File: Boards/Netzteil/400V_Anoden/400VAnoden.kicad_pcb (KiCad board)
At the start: 2 copper layers, 160 x 100 mm, 51 parts, among them P1 Drossel, P2 320V_AC, P3 Stabi, P4 133V_AC, P5 Stabi, P6 Trafo, P7 Trafo, P8 Relay, Q1 2SC2979

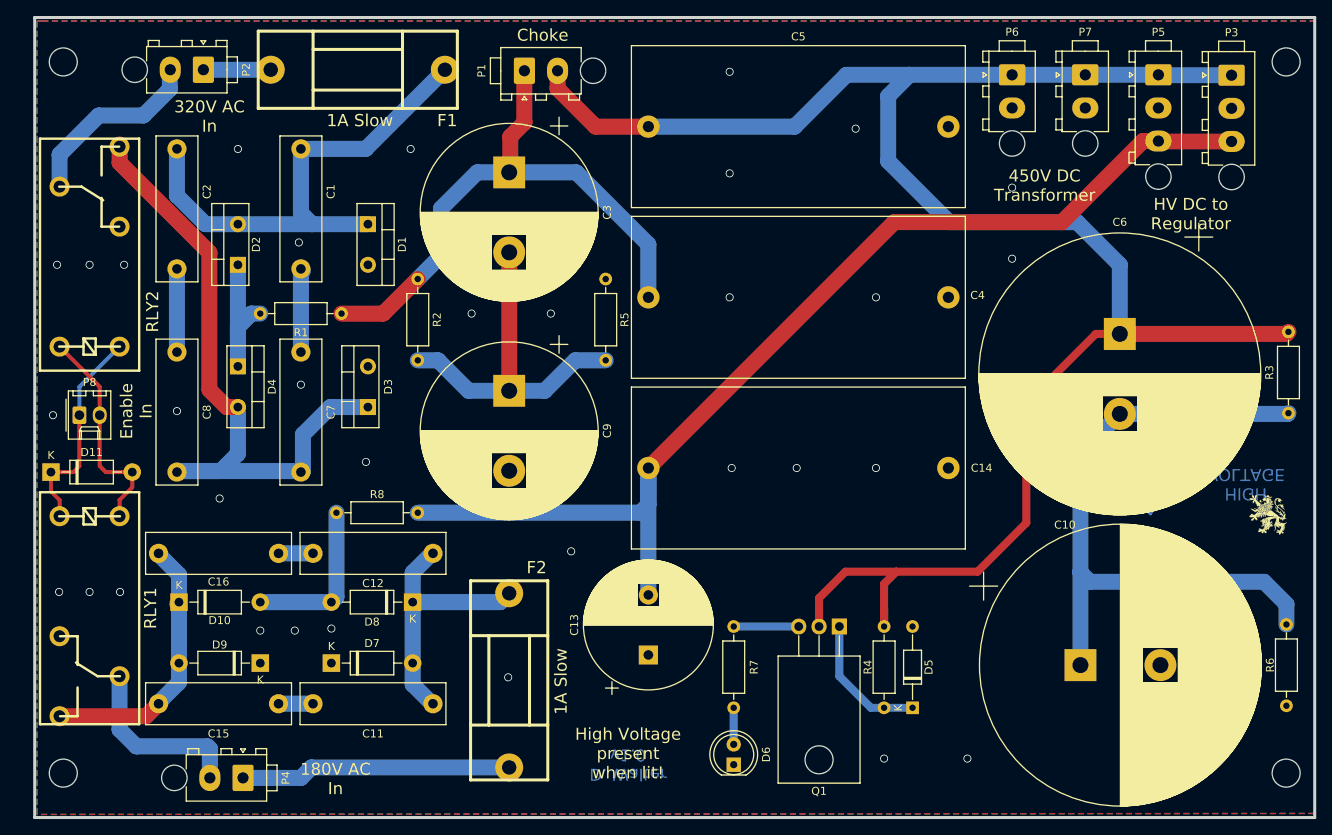
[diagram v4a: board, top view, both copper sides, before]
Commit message: Adjusted Silkscreen
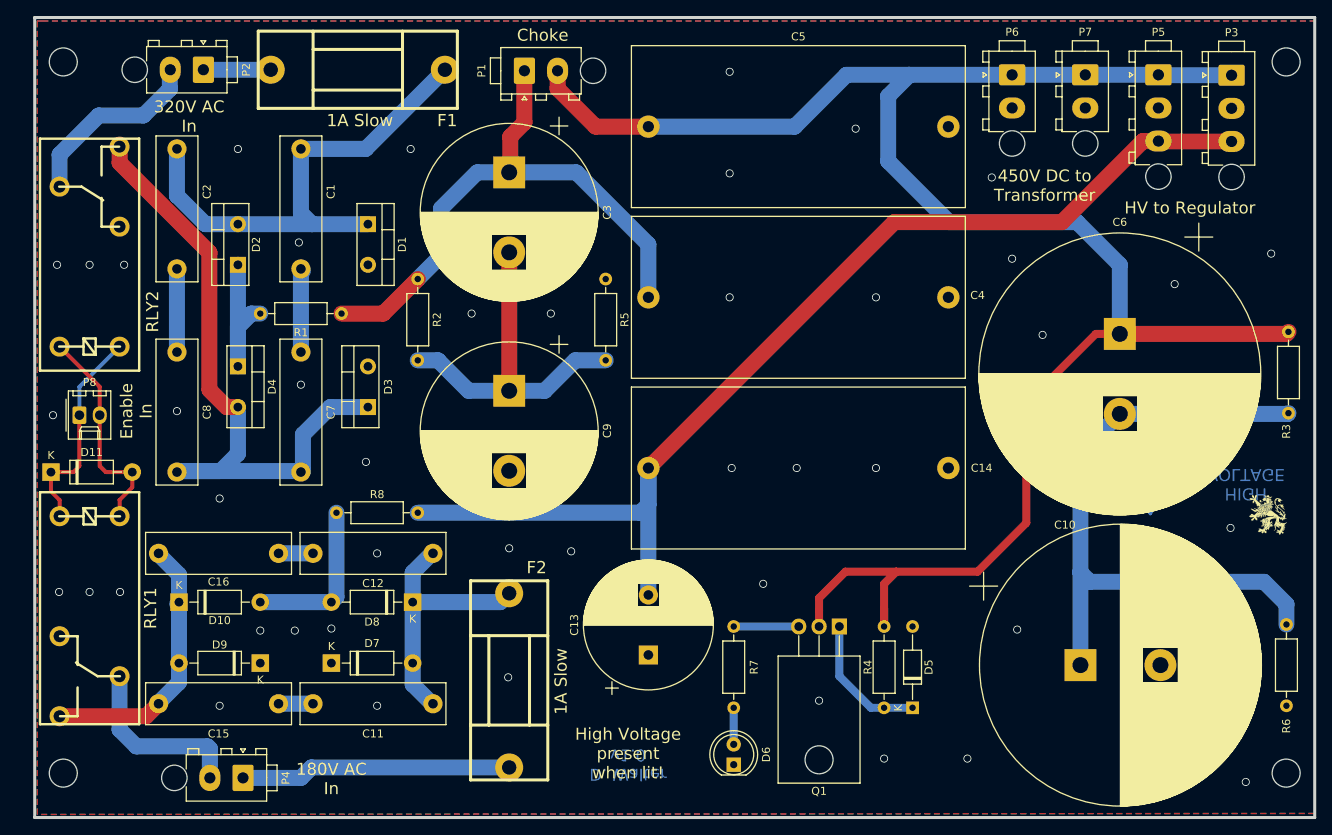
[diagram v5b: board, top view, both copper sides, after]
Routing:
- net GND: vias 33 -> 45
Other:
- board text added: "450V DC to Transformer"
- board text added: "HV to Regulator"
- board text removed: "450V DC Transformer"
- board text removed: "HV DC to Regulator"
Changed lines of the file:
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@@
     (thickness 1.6)
     (drawings 9)
-    (tracks 192)
+    (tracks 204)
     (zones 0)
     (modules 51)
@@
   (page A4)
   (layers
-    (0 F.Cu signal)
-    (31 B.Cu signal)
+    (0 F.Cu signal hide)
+    (31 B.Cu signal hide)
     (32 B.Adhes user)
     (33 F.Adhes user)
@@
     (descr "Resistor, Axial_DIN0207 series, Axial, Horizontal, pin pitch=10.16mm, 0.25W = 1/4W, length*diameter=6.3*2.5mm^2, http://cdn-reichelt.de/documents/datenblatt/B400/1_4W%23YAG.pdf")
     (tags "Resistor Axial_DIN0207 series Axial Horizontal pin pitch 10.16mm 0.25W = 1/4W length 6.3mm diameter 2.5mm")
-    (fp_text reference R6 (at 5.08 -2.032 90) (layer F.SilkS)
+    (fp_text reference R6 (at -2.54 0 90) (layer F.SilkS)
       (effects (font (size 1 1) (thickness 0.15)))
     )
@@
     (descr "Resistor, Axial_DIN0207 series, Axial, Horizontal, pin pitch=10.16mm, 0.25W = 1/4W, length*diameter=6.3*2.5mm^2, http://cdn-reichelt.de/documents/datenblatt/B400/1_4W%23YAG.pdf")
     (tags "Resistor Axial_DIN0207 series Axial Horizontal pin pitch 10.16mm 0.25W = 1/4W length 6.3mm diameter 2.5mm")
-    (fp_text reference R3 (at 5.08 -2.37 90) (layer F.SilkS)
+    (fp_text reference R3 (at -2.286 -0.254 90) (layer F.SilkS)
       (effects (font (size 1 1) (thickness 0.15)))
     )
@@
     )
   )
-  (gr_text "320V AC\nIn" (at 58.42 39.37) (layer F.SilkS)
+  (gr_text "320V AC\nIn" (at 55.88 39.37) (layer F.SilkS)
     (effects (font (size 1.5 1.5) (thickness 0.3)))
   )
-  (gr_text "180V AC\nIn" (at 74.168 122.174) (layer F.SilkS)
+  (gr_text "180V AC\nIn" (at 73.66 122.174) (layer F.SilkS)
     (effects (font (size 1.5 1.5) (thickness 0.3)))
   )
@@
     (effects (font (size 1.5 1.5) (thickness 0.3)))
   )
-  (gr_text "HV DC to\nRegulator" (at 181.102 51.562) (layer F.SilkS)
+  (gr_text "HV to Regulator" (at 180.975 50.8) (layer F.SilkS)
     (effects (font (size 1.5 1.5) (thickness 0.3)))
   )
-  (gr_text "450V DC\nTransformer" (at 162.814 48.006) (layer F.SilkS)
+  (gr_text "450V DC to\nTransformer" (at 162.814 48.006) (layer F.SilkS)
     (effects (font (size 1.5 1.5) (thickness 0.3)))
   )
@@
   (via (at 123.444 46.482) (size 1) (drill 0.8) (layers F.Cu B.Cu) (net 6))
   (via (at 123.444 33.782) (size 1) (drill 0.8) (layers F.Cu B.Cu) (net 6))
-  (via (at 158.75 48.26) (size 1) (drill 0.8) (layers F.Cu B.Cu) (net 6))
+  (via (at 156.21 46.99) (size 1) (drill 0.8) (layers F.Cu B.Cu) (net 6))
   (via (at 158.75 57.15) (size 1) (drill 0.8) (layers F.Cu B.Cu) (net 6))
   (via (at 64.77 103.632) (size 1) (drill 0.8) (layers F.Cu B.Cu) (net 6))
@@
   (via (at 153.162 119.634) (size 1) (drill 0.8) (layers F.Cu B.Cu) (net 6))
   (via (at 38.862 76.708) (size 1) (drill 0.8) (layers F.Cu B.Cu) (net 6))
+  (via (at 191.135 56.515) (size 1) (drill 0.8) (layers F.Cu B.Cu) (net 6))
+  (via (at 186.055 90.805) (size 1) (drill 0.8) (layers F.Cu B.Cu) (net 6))
+  (via (at 187.96 122.555) (size 1) (drill 0.8) (layers F.Cu B.Cu) (net 6))
+  (via (at 127.635 97.79) (size 1) (drill 0.8) (layers F.Cu B.Cu) (net 6))
+  (via (at 95.885 93.345) (size 1) (drill 0.8) (layers F.Cu B.Cu) (net 6))
+  (via (at 79.375 93.98) (size 1) (drill 0.8) (layers F.Cu B.Cu) (net 6))
+  (via (at 79.375 113.03) (size 1) (drill 0.8) (layers F.Cu B.Cu) (net 6))
+  (via (at 59.69 113.03) (size 1) (drill 0.8) (layers F.Cu B.Cu) (net 6))
+  (via (at 134.62 112.395) (size 1) (drill 0.8) (layers F.Cu B.Cu) (net 6))
+  (via (at 159.385 103.505) (size 1) (drill 0.8) (layers F.Cu B.Cu) (net 6))
+  (via (at 162.56 66.675) (size 1) (drill 0.8) (layers F.Cu B.Cu) (net 6))
+  (via (at 179.07 60.325) (size 1) (drill 0.8) (layers F.Cu B.Cu) (net 6))
   (segment (start 172.212 76.548) (end 167.292 81.468) (width 2) (layer B.Cu) (net 7) (status 10))
   (segment (start 193.2 76.548) (end 193.294 76.454) (width 2) (layer B.Cu) (net 7) (status 30))

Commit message: Added Mounting holes, Moved -60V Divider to HV Board, eliminated +450V Connector and Feedback Connector on Amp Board
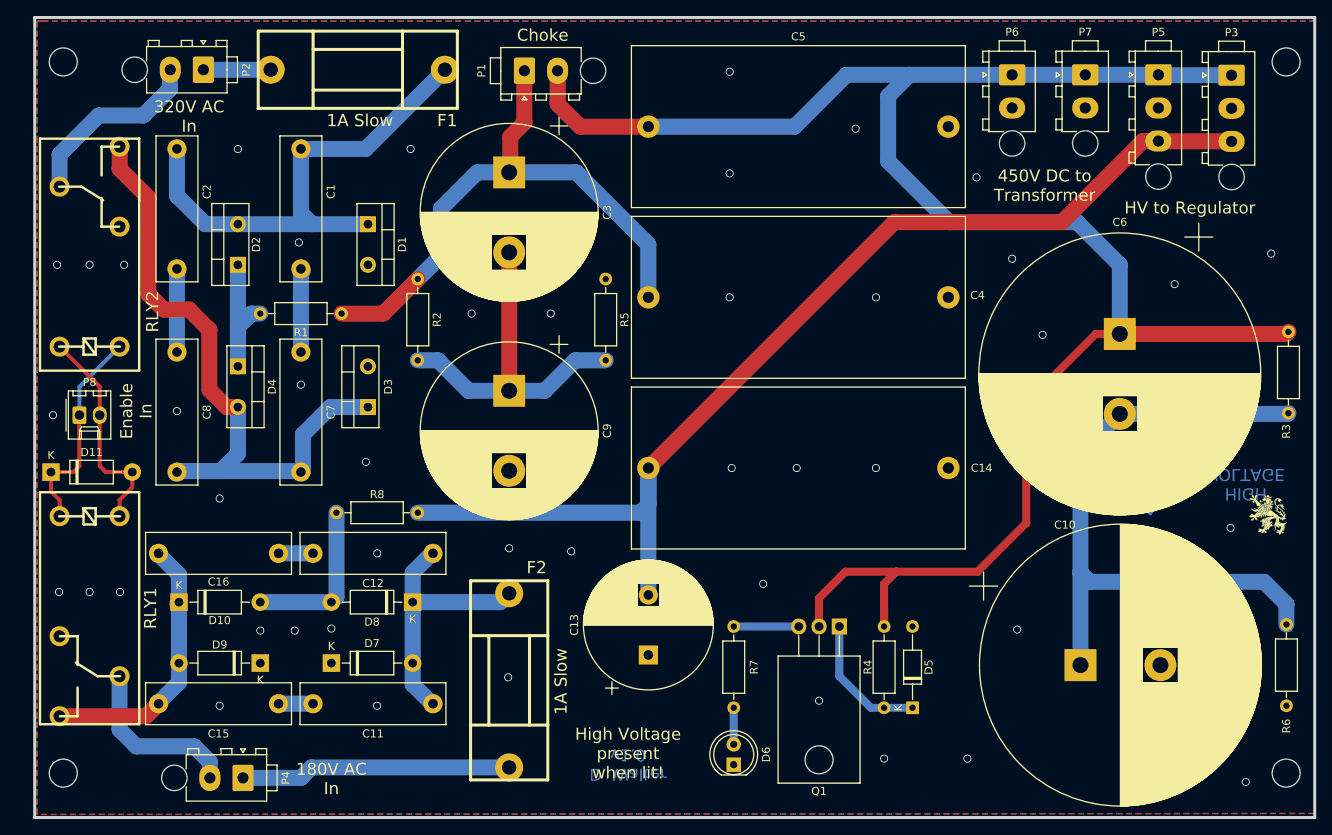
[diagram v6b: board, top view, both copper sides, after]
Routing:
- net Net-(C7-Pad2): track 83.7 -> 85.6 mm
- net /+450V_DC: track 240.0 -> 241.1 mm
- net Net-(P4-Pad2): track 22.6 -> 21.6 mm

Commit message: 6,3V und 12V auf einer Platine zusammengefasst
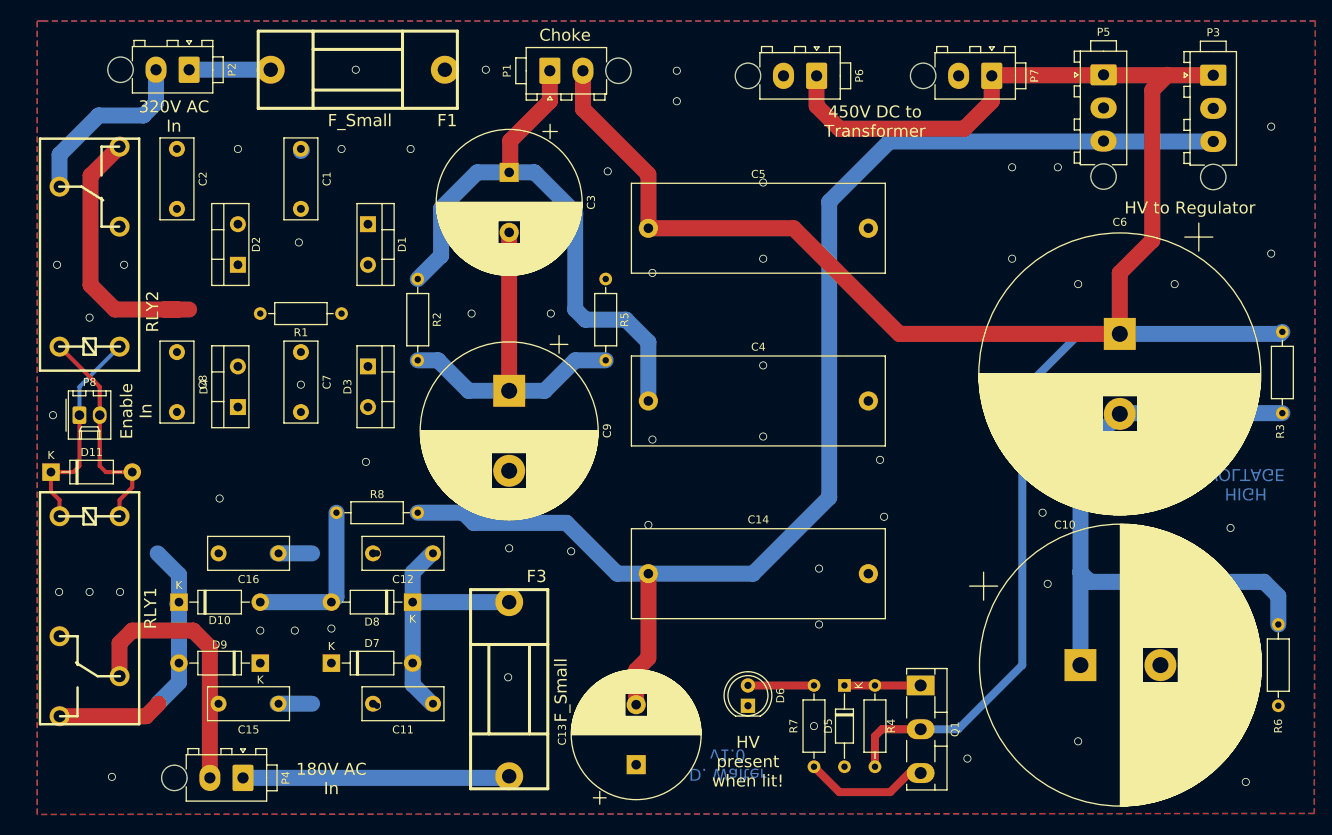
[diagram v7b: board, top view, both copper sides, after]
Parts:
- removed F2: 1A Slow, w_misc_comp:fuse_holder_CQ-2
- removed G***: LOGO, Loewe:Loewe_Klein
- removed REF**: Symbol_HighVoltage_Type2_CopperTop_VerySmall, Symbol:Symbol_HighVoltage_Type2_CopperTop_VerySmall
- removed REF**: EuroBoard160mmX100mm_holes, EuroBoard_Outline:EuroBoard160mmX100mm_holes
- added F3: F_Small, w_misc_comp:fuse_holder_CQ-2, F.Cu at (95.9, 111.0)
- C1, C11, C12, C15, C16, C2, C7, C8: value 1nF -> 1nF/450V; footprint Capacitor_THT:C_Rect_L18.0mm_W5.0mm_P15.00mm_FKS3_FKP3 -> Capacitor_THT:C_Rect_L10.0mm_W4.0mm_P7.50mm_FKS3_FKP3
- C14: value 1µF/600V -> 1µF/630V; footprint Capacitor_THT:C_Rect_L41.5mm_W20.0mm_P37.50mm_MKS4 -> Capacitor_THT:C_Rect_L31.5mm_W11.0mm_P27.50mm_MKS4
- C3: footprint Capacitor_THT:CP_Radial_D22.0mm_P10.00mm_SnapIn -> Capacitor_THT:CP_Radial_D18.0mm_P7.50mm
- C4, C5: footprint Capacitor_THT:C_Rect_L41.5mm_W20.0mm_P37.50mm_MKS4 -> Capacitor_THT:C_Rect_L31.5mm_W11.0mm_P27.50mm_MKS4
- F1: value 1A Slow -> F_Small
- Q1: footprint Package_TO_SOT_THT:TO-220-3_Horizontal_TabDown -> Package_TO_SOT_THT:TO-218-3_Vertical
- moved P6 24.4 mm to (134.3, 34.3), turned to 270 degrees
- moved C13 13.8 mm to (111.8, 120.4)
- moved C14 13.2 mm to (113.3, 96.5)
- moved C4 13.0 mm to (113.3, 74.9)
- moved C5 12.7 mm to (113.3, 53.3)
- moved Q1 12.5 mm to (147.3, 110.5), turned to 270 degrees
- moved P7 11.7 mm to (156.2, 34.3), turned to 270 degrees
- moved R7 10.4 mm to (134.0, 110.5), turned to 270 degrees
- moved D5 8.96 mm to (137.8, 110.5), turned to 270 degrees
- moved D6 7.58 mm to (125.7, 113.0)
- moved P5 6.86 mm to (170.2, 34.2)
- moved D3 5.08 mm to (78.2, 70.6), turned to 270 degrees
- moved D4 5.08 mm to (62.0, 75.7), turned to 90 degrees
- moved P1 3.17 mm to (101.0, 33.7)
- moved R4 3.02 mm to (141.6, 110.5), turned to 270 degrees
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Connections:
- RLY1 pad 12: Net-(RLY1-Pad12) -> (no net)
- RLY2 pad 12: Net-(RLY2-Pad12) -> (no net)
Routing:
- net Net-(C1-Pad1): track 63.3 -> 0.18 mm
- net Net-(C7-Pad2): track 85.6 -> 34.2 mm, vias 0 -> 1
- net /+450V_DC: track 241.1 -> 277.6 mm
- net /-180V_DC: track 139.5 -> 163.6 mm
- net Net-(D2-Pad1): track 18.1 -> 0.00 mm
- net Net-(P4-Pad2): track 21.6 -> 33.3 mm
- net Net-(C1-Pad2): track 10.6 -> 0.00 mm
- net Net-(C2-Pad2): track 10.4 -> 0.00 mm
- net Net-(Q1-Pad3): track 8.13 -> 15.6 mm
- net Net-(D5-Pad1): track 17.0 -> 9.53 mm
- net Net-(D6-Pad2): track 4.57 -> 8.26 mm
- net Net-(C3-Pad1): track 73.0 -> 75.8 mm
- net Net-(C3-Pad2): track 44.0 -> 46.5 mm
- net Net-(F1-Pad1): track 8.42 -> 10.2 mm
- net Net-(C10-Pad1): track 84.5 -> 83.3 mm
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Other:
- board outline removed
- board text added: "HV present when lit!"
- board text removed: "High Voltage present when lit!"

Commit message: Reworked Delay + Layout changed
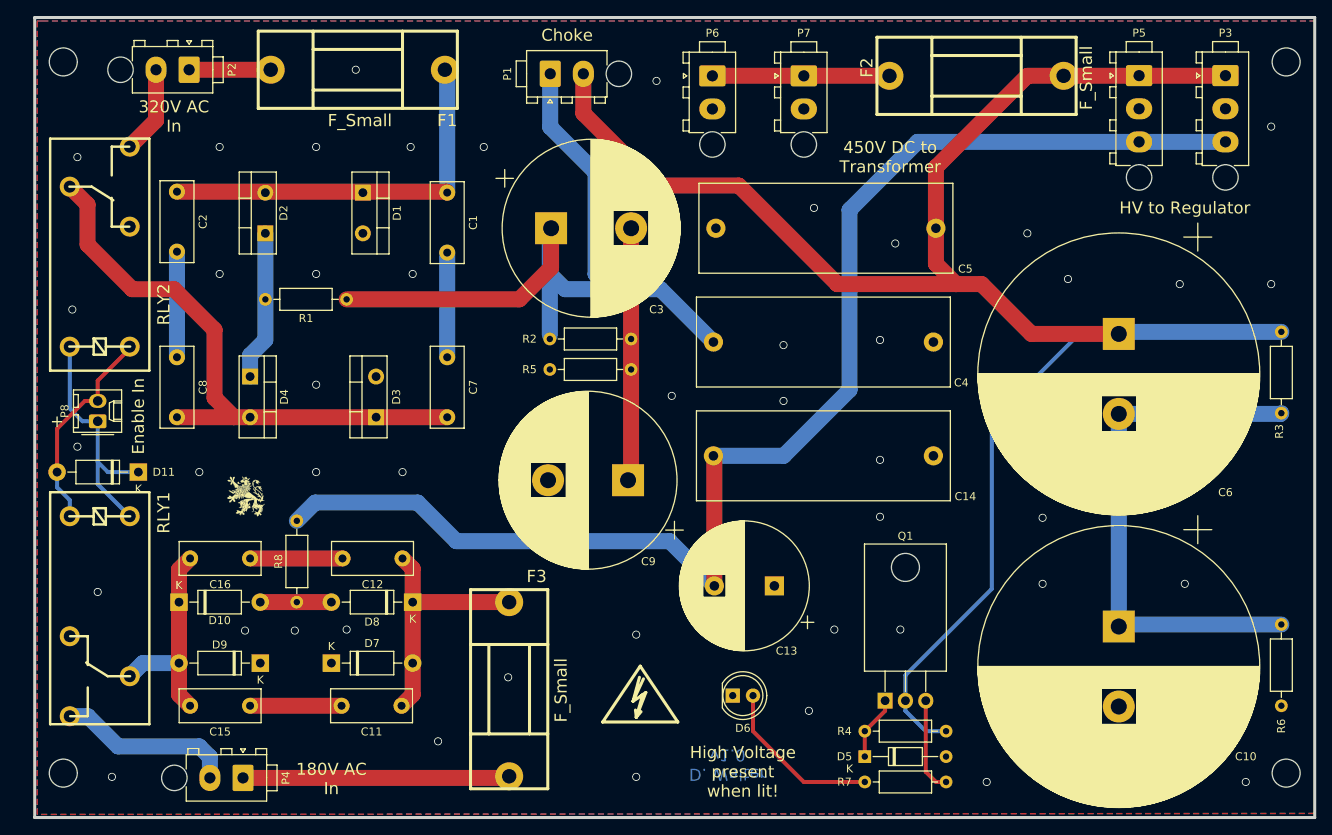
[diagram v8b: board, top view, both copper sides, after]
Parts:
- added F2: F_Small, w_misc_comp:fuse_holder_CQ-2, F.Cu at (154.3, 34.3)
- added G***: LOGO, Loewe:Loewe_Klein, F.Cu at (63.0, 86.9)
- added REF**: Symbol_HighVoltage_Type2_SilkTop_VerySmall, Loewe:Symbol_HighVoltage_Type2_SilkTop_VerySmall, F.Cu at (112.3, 112.3)
- added REF**: EuroBoard160mmX100mm_holes, EuroBoard_Outline:EuroBoard160mmX100mm_holes, F.Cu at (36.6, 127.0)
- C3: footprint Capacitor_THT:CP_Radial_D18.0mm_P7.50mm -> Capacitor_THT:CP_Radial_D22.0mm_P10.00mm_SnapIn
- Q1: footprint Package_TO_SOT_THT:TO-218-3_Vertical -> Package_TO_SOT_THT:TO-220-3_Horizontal_TabDown
- moved C5 35.9 mm to (149.2, 53.3), turned to 180 degrees
- moved C13 28.2 mm to (129.0, 98.0), turned to 180 degrees
- moved R2 26.8 mm to (111.1, 67.2), turned to 180 degrees
- moved P7 23.5 mm to (132.7, 34.3), turned to 0 degrees
- moved C1 19.1 mm to (88.1, 48.9)
- moved C9 18.6 mm to (110.7, 84.8), turned to 180 degrees
- moved C7 18.3 mm to (88.1, 69.5)
- moved C14 16.8 mm to (121.4, 81.8)
- moved R8 15.1 mm to (69.3, 89.9), turned to 270 degrees
- moved R7 13.6 mm to (140.3, 122.6), turned to 0 degrees
- moved R5 13.3 mm to (101.0, 71.0), turned to 0 degrees
- moved P6 13.0 mm to (121.3, 34.3), turned to 0 degrees
- moved C4 11.0 mm to (121.4, 67.6)
- moved D11 10.9 mm to (49.5, 83.8), turned to 180 degrees
- moved D5 9.25 mm to (140.3, 119.4), turned to 0 degrees
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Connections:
- C5 pad 1: /+450V_DC -> Net-(C5-Pad1)
- C6 pad 1: /+450V_DC -> Net-(C5-Pad1)
- P1 pad 2: /+450V_DC -> Net-(C5-Pad1)
- P3 pad 1: /+450V_DC -> Net-(C5-Pad1)
- P5 pad 1: /+450V_DC -> Net-(C5-Pad1)
- Q1 pad 2: /+450V_DC -> Net-(C5-Pad1)
- R3 pad 2: /+450V_DC -> Net-(C5-Pad1)
- R4 pad 2: /+450V_DC -> Net-(C5-Pad1)
- RLY1 pad 1: Net-(D11-Pad1) -> Net-(D11-Pad2)
- RLY1 pad 11: Net-(P4-Pad2) -> Net-(C15-Pad2)
- RLY1 pad 14: Net-(C15-Pad2) -> Net-(P4-Pad2)
- RLY1 pad 2: Net-(D11-Pad2) -> Net-(D11-Pad1)
- RLY2 pad 1: Net-(D11-Pad1) -> Net-(D11-Pad2)
- RLY2 pad 11: Net-(P2-Pad2) -> Net-(C7-Pad2)
- RLY2 pad 14: Net-(C7-Pad2) -> Net-(P2-Pad2)
- RLY2 pad 2: Net-(D11-Pad2) -> Net-(D11-Pad1)
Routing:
- net /+450V_DC: track 277.6 -> 22.1 mm
- net Net-(C5-Pad1): track 0.00 -> 227.6 mm
- net Net-(C1-Pad1): track 0.18 -> 49.3 mm
- net Net-(C7-Pad2): track 34.2 -> 74.1 mm, vias 1 -> 0
- net Net-(C3-Pad1): track 75.8 -> 99.6 mm
- net Net-(D2-Pad1): track 0.00 -> 18.7 mm
- net Net-(C3-Pad2): track 46.5 -> 30.5 mm
- net Net-(C10-Pad1): track 83.3 -> 67.7 mm
- net Net-(C2-Pad2): track 0.00 -> 13.2 mm
- net Net-(C1-Pad2): track 0.00 -> 13.1 mm
- net Net-(D6-Pad2): track 8.26 -> 21.0 mm
- net Net-(P2-Pad2): track 22.9 -> 11.0 mm
- net Net-(D10-Pad2): track 20.3 -> 8.89 mm
- net Net-(P4-Pad2): track 33.3 -> 22.2 mm
- net Net-(C15-Pad2): track 34.3 -> 26.4 mm, vias 1 -> 0
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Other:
- board outline added: 160 x 100 mm
- board text added: "+"
- board text added: "High Voltage present when lit!"
- board text removed: "HIGH VOLTAGE"
- board text removed: "HV present when lit!"
